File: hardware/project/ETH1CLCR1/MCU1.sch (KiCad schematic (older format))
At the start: 42 parts, among them J301 Conn_02x01, J302 20021111-00010T4LF, U301 STM32F765ZGT6, U302 24LC08B-E/MS, U303 HDC1080, Y301 NX3225GD-8MHZ-STD-CRA-3

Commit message: SCPI function development.
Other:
- note added: "MCU1_GPIO_OUT1 = MCU1_TX_DATA\nMCU1_GPIO_OUT2 = MCU1_RX_DATA\nMCU1_STATUS_IN1 = MCU2_RX_STATUS\n"
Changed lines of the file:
@@
 Text HLabel 14600 5400 2    50   Input ~ 0
 MCU1_STATUS_IN1
-Text HLabel 14600 5500 2    50   Output ~ 0
-MCU1_GPIO_OUT2
-Text HLabel 14600 5600 2    50   Output ~ 0
-MCU1_GPIO_OUT1
 Wire Wire Line
 	14600 5500 14550 5500
@@
 NoConn ~ 14550 7800
 NoConn ~ 3150 4400
+Text HLabel 14600 5500 2    50   Output ~ 0
+MCU1_GPIO_OUT2
+Text HLabel 14600 5600 2    50   Output ~ 0
+MCU1_GPIO_OUT1
+Text Notes 12400 9650 0    50   ~ 0
+MCU1_GPIO_OUT1 = MCU1_TX_DATA\nMCU1_GPIO_OUT2 = MCU1_RX_DATA\nMCU1_STATUS_IN1 = MCU2_RX_STATUS\n
 $EndSCHEMATC

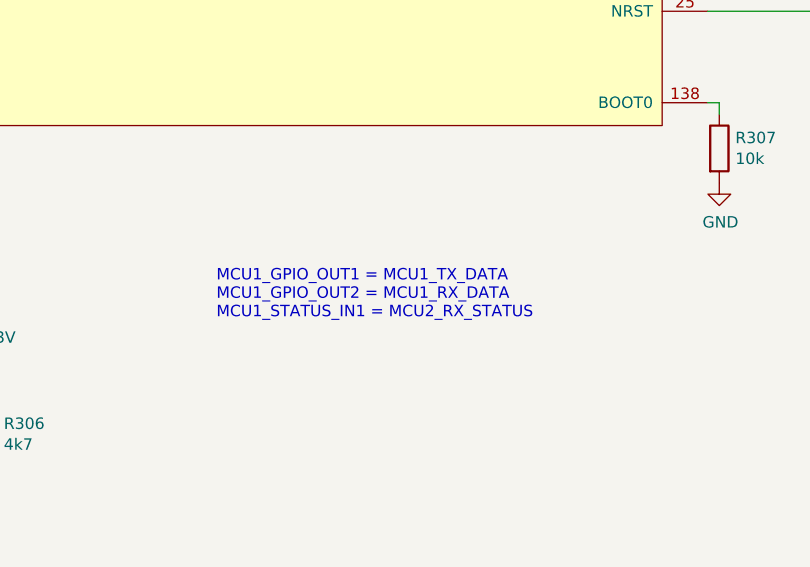
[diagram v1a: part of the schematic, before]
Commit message: MCU1 SCPI functions development.
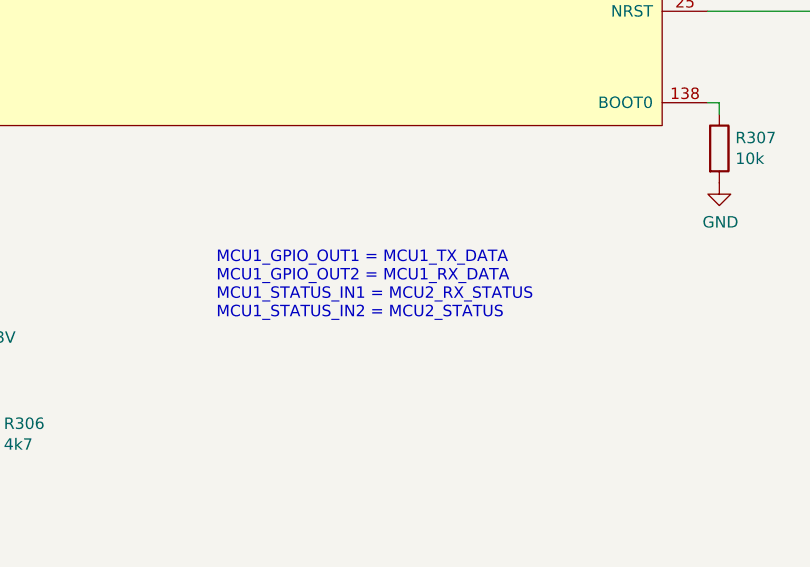
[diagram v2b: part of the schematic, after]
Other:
- note added: "MCU1_GPIO_OUT1 = MCU1_TX_DATA\nMCU1_GPIO_OUT2 = MCU1_RX_DATA\nMCU1_STATUS_IN1 = MCU2_RX_STATUS\nMCU1_STATUS_IN2 = MCU2_STATUS"
- note removed: "MCU1_GPIO_OUT1 = MCU1_TX_DATA\nMCU1_GPIO_OUT2 = MCU1_RX_DATA\nMCU1_STATUS_IN1 = MCU2_RX_STATUS\n"
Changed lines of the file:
@@
 MCU1_GPIO_OUT1
 Text Notes 12400 9650 0    50   ~ 0
-MCU1_GPIO_OUT1 = MCU1_TX_DATA\nMCU1_GPIO_OUT2 = MCU1_RX_DATA\nMCU1_STATUS_IN1 = MCU2_RX_STATUS\n
+MCU1_GPIO_OUT1 = MCU1_TX_DATA\nMCU1_GPIO_OUT2 = MCU1_RX_DATA\nMCU1_STATUS_IN1 = MCU2_RX_STATUS\nMCU1_STATUS_IN2 = MCU2_STATUS
 $EndSCHEMATC
